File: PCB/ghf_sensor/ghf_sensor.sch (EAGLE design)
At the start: 14 parts, among them IC1 MAX481CPA, J1 MH-Z19-CO2-NDIR-SENSOR, T1 BPX81, X1 SoilSens, X2 RS485

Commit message: PCB modified
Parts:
- removed R5: (no value), resistor:R-EU_0204/7
- added R6: 10k, rcl:R-US_0204/5
- added R7: 4.7k, rcl:R-US_0204/5
- added R8: 100, rcl:R-US_0204/5
- added T2: (no value), transistor:-NPN-TO92
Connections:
- removed net N$12: R5.1, X2-1.KL
- new net N$13: IC1G$1.DE, IC1G$1.RE/, R6.2, T2.C
- new net N$14: R7.2, T2.B
- new net N$15: IC1G$1.DI, R7.1, U$2.TX0
- new net N$16: R8.2, U$2.A1
- net +5V: now also R6.1, U$1.VCC, X2-1.KL; no longer R5.2
- net GND: now also T2.E
- net N$8: now also R8.1, X1-3.KL; no longer IC1G$1.DI, U$2.TX0
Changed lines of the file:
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@@
 <part name="R4" library="varistor" deviceset="VARISTOR" device="CN1812" value="VARISTORCN1812"/>
 <part name="SUPPLY14" library="supply2" deviceset="+5V" device=""/>
-<part name="R5" library="resistor" deviceset="R-EU_" device="0204/7"/>
+<part name="T2" library="transistor" deviceset="*-NPN-" device="TO92"/>
+<part name="R6" library="rcl" deviceset="R-US_" device="0204/5" value="10k"/>
+<part name="R7" library="rcl" deviceset="R-US_" device="0204/5" value="4.7k"/>
+<part name="SUPPLY15" library="supply2" deviceset="GND" device=""/>
+<part name="SUPPLY16" library="supply2" deviceset="+5V" device=""/>
+<part name="R8" library="rcl" deviceset="R-US_" device="0204/5" value="100"/>
+<part name="SUPPLY17" library="supply2" deviceset="+5V" device=""/>
 </parts>
 <sheets>
@@
 <instance part="U$3" gate="A" x="134.62" y="17.78"/>
 <instance part="U$4" gate="A" x="134.62" y="22.86"/>
-<instance part="SUPPLY13" gate="+5V" x="139.7" y="30.48"/>
+<instance part="SUPPLY13" gate="+5V" x="129.54" y="30.48"/>
 <instance part="R4" gate="G$1" x="147.32" y="35.56"/>
 <instance part="SUPPLY14" gate="+5V" x="53.34" y="33.02"/>
-<instance part="R5" gate="G$1" x="132.08" y="27.94"/>
+<instance part="T2" gate="G$1" x="119.38" y="86.36"/>
+<instance part="R6" gate="G$1" x="121.92" y="99.06" rot="R270"/>
+<instance part="R7" gate="G$1" x="109.22" y="88.9"/>
+<instance part="SUPPLY15" gate="GND" x="121.92" y="78.74"/>
+<instance part="SUPPLY16" gate="+5V" x="121.92" y="106.68"/>
+<instance part="R8" gate="G$1" x="58.42" y="20.32"/>
+<instance part="SUPPLY17" gate="+5V" x="78.74" y="40.64"/>
 </instances>
 <busses>
@@
 <pinref part="SUPPLY8" gate="GND" pin="GND"/>
 <wire x1="119.38" y1="40.64" x2="114.3" y2="40.64" width="0.1524" layer="91"/>
+</segment>
+<segment>
+<pinref part="T2" gate="G$1" pin="E"/>
+<pinref part="SUPPLY15" gate="GND" pin="GND"/>
 </segment>
 </net>
@@
 </segment>
 <segment>
-<pinref part="R5" gate="G$1" pin="2"/>
+<pinref part="R6" gate="G$1" pin="1"/>
+<pinref part="SUPPLY16" gate="+5V" pin="+5V"/>
+</segment>
+<segment>
+<pinref part="SUPPLY17" gate="+5V" pin="+5V"/>
+<wire x1="78.74" y1="38.1" x2="78.74" y2="33.02" width="0.1524" layer="91"/>
+<pinref part="U$1" gate="G$1" pin="VCC"/>
+<wire x1="78.74" y1="33.02" x2="81.28" y2="33.02" width="0.1524" layer="91"/>
+</segment>
+<segment>
+<pinref part="X2" gate="-1" pin="KL"/>
 <pinref part="SUPPLY13" gate="+5V" pin="+5V"/>
-<wire x1="137.16" y1="27.94" x2="139.7" y2="27.94" width="0.1524" layer="91"/>
+<wire x1="129.54" y1="27.94" x2="124.46" y2="27.94" width="0.1524" layer="91"/>
 </segment>
 </net>
@@
 <wire x1="-22.86" y1="53.34" x2="-27.94" y2="53.34" width="0.1524" layer="91"/>
 <wire x1="-27.94" y1="53.34" x2="-27.94" y2="83.82" width="0.1524" layer="91"/>
-<wire x1="-27.94" y1="83.82" x2="81.28" y2="83.82" width="0.1524" layer="91"/>
-<wire x1="81.28" y1="83.82" x2="81.28" y2="55.88" width="0.1524" layer="91"/>
+<wire x1="-27.94" y1="83.82" x2="78.74" y2="83.82" width="0.1524" layer="91"/>
+<wire x1="78.74" y1="83.82" x2="78.74" y2="55.88" width="0.1524" layer="91"/>
 <pinref part="J1" gate="G$1" pin="TX"/>
-<wire x1="81.28" y1="55.88" x2="76.2" y2="55.88" width="0.1524" layer="91"/>
+<wire x1="78.74" y1="55.88" x2="76.2" y2="55.88" width="0.1524" layer="91"/>
 </segment>
 </net>
@@
 <segment>
 <pinref part="J1" gate="G$1" pin="RX"/>
-<wire x1="76.2" y1="53.34" x2="83.82" y2="53.34" width="0.1524" layer="91"/>
-<wire x1="83.82" y1="53.34" x2="83.82" y2="86.36" width="0.1524" layer="91"/>
-<wire x1="83.82" y1="86.36" x2="-30.48" y2="86.36" width="0.1524" layer="91"/>
+<wire x1="76.2" y1="53.34" x2="81.28" y2="53.34" width="0.1524" layer="91"/>
+<wire x1="81.28" y1="53.34" x2="81.28" y2="86.36" width="0.1524" layer="91"/>
+<wire x1="81.28" y1="86.36" x2="-30.48" y2="86.36" width="0.1524" layer="91"/>
 <wire x1="-30.48" y1="86.36" x2="-30.48" y2="50.8" width="0.1524" layer="91"/>
 <pinref part="U$2" gate="G$1" pin="D5"/>
@@
 </segment>
 </net>
-<net name="N$8" class="0">
-<segment>
-<pinref part="U$2" gate="G$1" pin="TX0"/>
-<wire x1="-22.86" y1="68.58" x2="-25.4" y2="68.58" width="0.1524" layer="91"/>
-<wire x1="-25.4" y1="68.58" x2="-25.4" y2="88.9" width="0.1524" layer="91"/>
-<wire x1="-25.4" y1="88.9" x2="86.36" y2="88.9" width="0.1524" layer="91"/>
-<wire x1="86.36" y1="88.9" x2="86.36" y2="53.34" width="0.1524" layer="91"/>
-<pinref part="IC1" gate="G$1" pin="DI"/>
-<wire x1="86.36" y1="53.34" x2="91.44" y2="53.34" width="0.1524" layer="91"/>
-</segment>
-</net>
 <net name="N$9" class="0">
 <segment>
@@
 <wire x1="-22.86" y1="66.04" x2="-33.02" y2="66.04" width="0.1524" layer="91"/>
 <wire x1="-33.02" y1="66.04" x2="-33.02" y2="91.44" width="0.1524" layer="91"/>
-<wire x1="-33.02" y1="91.44" x2="88.9" y2="91.44" width="0.1524" layer="91"/>
-<wire x1="88.9" y1="91.44" x2="88.9" y2="68.58" width="0.1524" layer="91"/>
+<wire x1="-33.02" y1="91.44" x2="86.36" y2="91.44" width="0.1524" layer="91"/>
+<wire x1="86.36" y1="91.44" x2="86.36" y2="68.58" width="0.1524" layer="91"/>
 <pinref part="IC1" gate="G$1" pin="RO"/>
-<wire x1="88.9" y1="68.58" x2="91.44" y2="68.58" width="0.1524" layer="91"/>
+<wire x1="86.36" y1="68.58" x2="91.44" y2="68.58" width="0.1524" layer="91"/>
 </segment>
 </net>
@@
 </segment>
 </net>
-<net name="N$12" class="0">
-<segment>
-<pinref part="X2" gate="-1" pin="KL"/>
-<pinref part="R5" gate="G$1" pin="1"/>
-<wire x1="127" y1="27.94" x2="124.46" y2="27.94" width="0.1524" layer="91"/>
-</segment>
-</net>
+<net name="N$13" class="0">
+<segment>
+<pinref part="T2" gate="G$1" pin="C"/>
+<pinref part="R6" gate="G$1" pin="2"/>
+<wire x1="121.92" y1="93.98" x2="121.92" y2="91.44" width="0.1524" layer="91"/>
+<pinref part="IC1" gate="G$1" pin="RE/"/>
+<wire x1="91.44" y1="63.5" x2="88.9" y2="63.5" width="0.1524" layer="91"/>
+<pinref part="IC1" gate="G$1" pin="DE"/>
+<wire x1="91.44" y1="58.42" x2="88.9" y2="58.42" width="0.1524" layer="91"/>
+<wire x1="88.9" y1="58.42" x2="88.9" y2="63.5" width="0.1524" layer="91"/>
+<wire x1="88.9" y1="63.5" x2="88.9" y2="93.98" width="0.1524" layer="91"/>
+<wire x1="88.9" y1="93.98" x2="121.92" y2="93.98" width="0.1524" layer="91"/>
+<junction x="88.9" y="63.5"/>
+</segment>
+</net>
+<net name="N$14" class="0">
+<segment>
+<pinref part="T2" gate="G$1" pin="B"/>
+<pinref part="R7" gate="G$1" pin="2"/>
+<wire x1="114.3" y1="88.9" x2="116.84" y2="86.36" width="0.1524" layer="91"/>
+</segment>
+</net>
+<net name="N$15" class="0">
+<segment>
+<pinref part="R7" gate="G$1" pin="1"/>
+<wire x1="83.82" y1="88.9" x2="104.14" y2="88.9" width="0.1524" layer="91"/>
+<pinref part="U$2" gate="G$1" pin="TX0"/>
+<wire x1="-22.86" y1="68.58" x2="-25.4" y2="68.58" width="0.1524" layer="91"/>
+<wire x1="-25.4" y1="68.58" x2="-25.4" y2="88.9" width="0.1524" layer="91"/>
+<wire x1="-25.4" y1="88.9" x2="83.82" y2="88.9" width="0.1524" layer="91"/>
+<wire x1="83.82" y1="88.9" x2="83.82" y2="53.34" width="0.1524" layer="91"/>
+<pinref part="IC1" gate="G$1" pin="DI"/>
+<wire x1="83.82" y1="53.34" x2="91.44" y2="53.34" width="0.1524" layer="91"/>
+<junction x="83.82" y="88.9"/>
+</segment>
+</net>
+<net name="N$8" class="0">
+<segment>
+<pinref part="X1" gate="-3" pin="KL"/>
+<pinref part="R8" gate="G$1" pin="1"/>
+</segment>
+</net>
+<net name="N$16" class="0">
+<segment>
+<pinref part="U$2" gate="G$1" pin="A1"/>
+<wire x1="20.32" y1="53.34" x2="27.94" y2="53.34" width="0.1524" layer="91"/>
+<wire x1="27.94" y1="53.34" x2="27.94" y2="38.1" width="0.1524" layer="91"/>
+<wire x1="27.94" y1="38.1" x2="55.88" y2="38.1" width="0.1524" layer="91"/>
+<wire x1="55.88" y1="38.1" x2="55.88" y2="27.94" width="0.1524" layer="91"/>
+<pinref part="R8" gate="G$1" pin="2"/>
+<wire x1="55.88" y1="27.94" x2="63.5" y2="27.94" width="0.1524" layer="91"/>
+<wire x1="63.5" y1="27.94" x2="63.5" y2="20.32" width="0.1524" layer="91"/>
+</segment>
+</net>

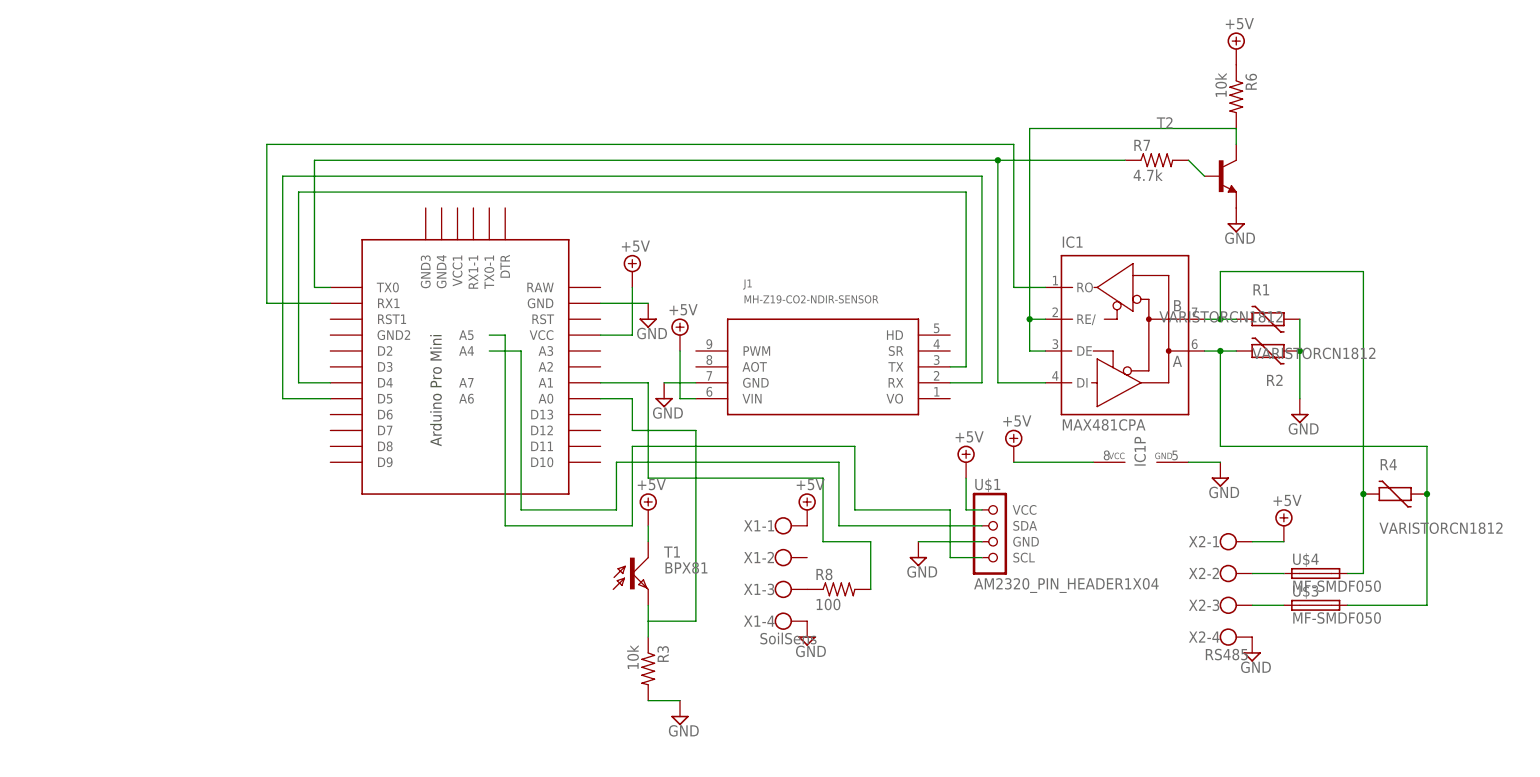
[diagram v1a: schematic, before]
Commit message: add cad data, modify PCB board and schematic
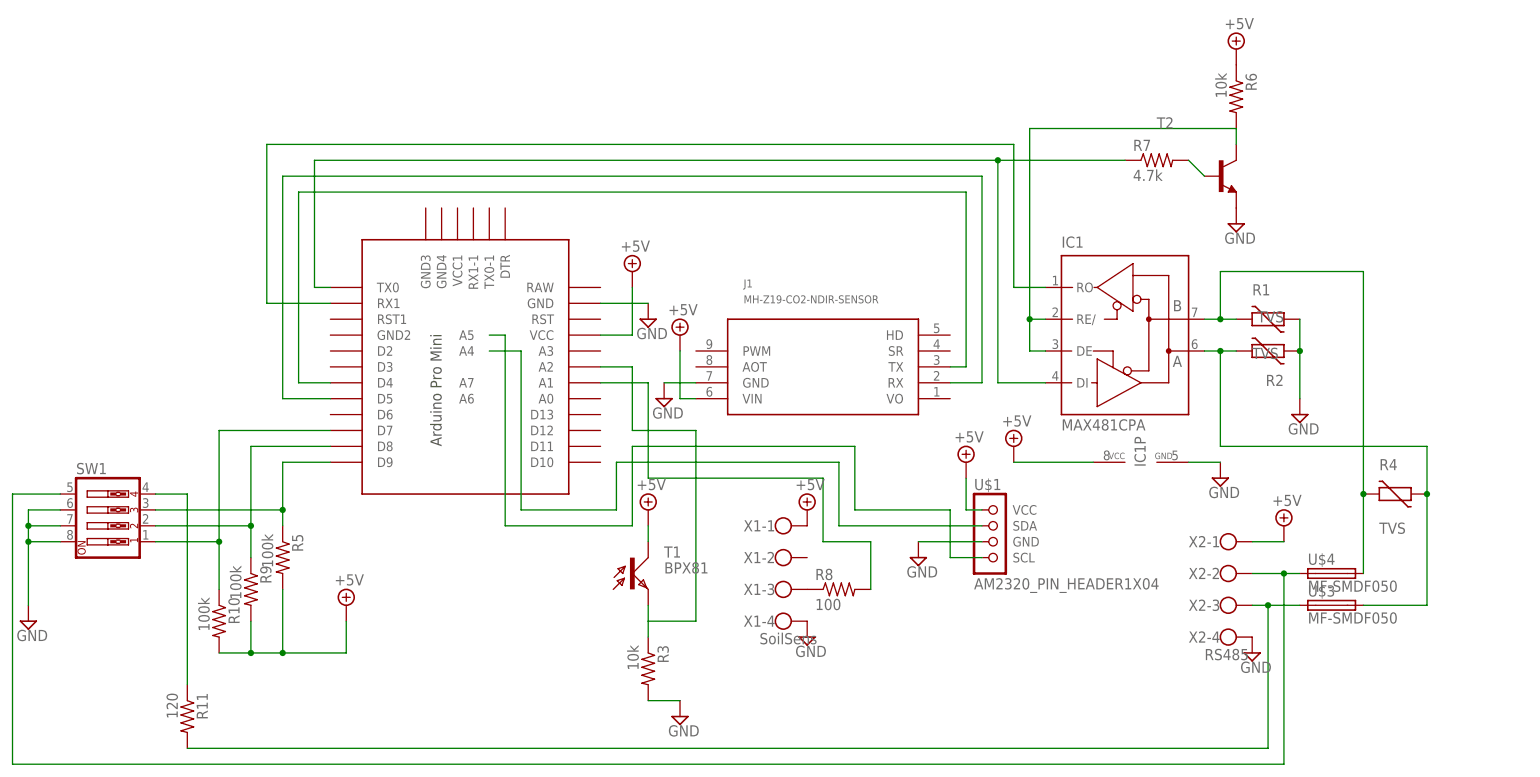
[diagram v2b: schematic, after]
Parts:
- added R10, R5, R9: 100k, rcl:R-US_0204/2V
- added R11: 120, rcl:R-US_0204/2V
- added SW1: (no value), special:SW_DIP-4
- R1, R2, R4: value VARISTORCN1812 -> TVS
- R3: device rcl:R-US_0204/7 -> rcl:R-US_0204/5
- T2: device transistor:-NPN-TO92 -> transistor:-NPN-TO92-ECB
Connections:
- removed net N$4: U$4.1, X2-2.KL
- removed net N$5: U$3.1, X2-3.KL
- new net N$12: R5.1, SW1.3, U$2.D9
- new net N$18: R9.1, SW1.2, U$2.D8
- new net N$19: R10.1, SW1.1, U$2.D7
- new net N$2: SW1.5, U$4.1, X2-2.KL
- new net N$20: R11.1, SW1.4
- new net N$3: R11.2, U$3.1, X2-3.KL
- net +5V: now also R10.2, R5.2, R9.2
- net GND: now also SW1.6, SW1.7, SW1.8
- net N$1: now also U$2.A2; no longer U$2.A0
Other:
- moved on the sheet: U$3, U$4
